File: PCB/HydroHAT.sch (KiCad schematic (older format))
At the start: 13 parts, among them IC1 ATMEGA1284P-P, P1 CONN_20X2, P2 CONN_4, P3 CONN_4, P4 CONN_10X2, P5 CONN_8, P6 CONN_4, SW1 SW_PUSH

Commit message: Changed Things
Stuff
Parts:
- removed P2, P3: CONN_4, symbol CONN_4
- added P2, P3: CONN_3, symbol CONN_3
- RES?: value RESONATOR_C -> 20MHz; Distrib Link (none) -> 490-1215-ND; Distrib PN (none) -> 490-1215-ND; MFG Name (none) -> Murata Electronics North America; MFG Part Num (none) -> CSTLS20M0X53-B0
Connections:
- net GND: now also P2.2 (PM), P3.2 (PM)
- net at IC1.22 ((PCINT16/SCL)PC0): now also P2.1 (P1)
- net at IC1.23 ((PCINT17/SDA)PC1): now also P2.3 (P3)
- net Vdd: now reaches P1.17 (P17)
- net at P1.3 (P3): now also P3.3 (P3)
- net at P1.5 (P5): now also P3.1 (P1)
- net MISO renamed MISO33
- net MISO33: no longer IC1.7 ((PCINT14/MISO)PB6)
- net MOSI renamed MOSI33
- net MOSI33: no longer IC1.6 ((PCINT13/MOSI)PB5)
- net SCK renamed SCK33
- net SCK33: no longer IC1.8 ((PCINT15/SCK)PB7)
- new net MISO50: IC1.7 ((PCINT14/MISO)PB6)
- new net MOSI50: IC1.6 ((PCINT13/MOSI)PB5)
- new net SCK50: IC1.8 ((PCINT15/SCK)PB7)
- no-connect marks 28 -> 27
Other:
- note added: "5V\nGPIO Port"
- note added: "To RPi\n 3.3V\n\n"
- note removed: "GPIO Port"
- note removed: "To RPi\n"
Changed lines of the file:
@@
 $EndComp
 Text Notes 9200 6200 0    60   ~ 12
-To RPi\n
+To RPi\n 3.3V\n\n
 Text GLabel 6350 4750 2    60   Input ~ 0
 RXD
@@
 P 4000 2650
 F 0 "RES?" H 4000 3000 60  0000 C CNN
-F 1 "RESONATOR_C" H 4000 2300 60  0000 C CNN
+F 1 "20MHz" H 4000 2300 60  0000 C CNN
 F 2 "" H 4000 3050 60  0000 C CNN
-F 3 "" H 4000 3050 60  0000 C CNN
+F 3 "http://www.murata.com/~/media/webrenewal/support/library/catalog/products/timingdevice/ceralock/p16e.ashx" H 4000 3050 60  0001 C CNN
+F 4 "Murata Electronics North America" H 4000 2650 60  0001 C CNN "MFG Name"
+F 5 "CSTLS20M0X53-B0" H 4000 2650 60  0001 C CNN "MFG Part Num"
+F 6 "490-1215-ND" H 4000 2650 60  0001 C CNN "Distrib PN"
+F 7 "490-1215-ND" H 4000 2650 60  0001 C CNN "Distrib Link"
 	1    4000 2650
 	1    0    0    -1
@@
 Text Notes 6900 5300 0    60   ~ 0
 Aux Serial Port
-Text Notes 6750 1750 0    60   ~ 0
-GPIO Port
-$Comp
-L CONN_4 P2
-U 1 1 5420C6D0
-P 7250 3900
-F 0 "P2" V 7200 3900 50  0000 C CNN
-F 1 "CONN_4" V 7300 3900 50  0000 C CNN
-F 2 "" H 7250 3900 60  0000 C CNN
-F 3 "" H 7250 3900 60  0000 C CNN
-	1    7250 3900
-	1    0    0    -1
-$EndComp
+Text Notes 6650 1750 0    60   ~ 0
+   5V\nGPIO Port
 Text Notes 6950 3650 0    60   ~ 0
 I2C Port
 Text GLabel 6350 3450 2    60   Input ~ 0
-MOSI
+MOSI50
 Text GLabel 6350 3550 2    60   Input ~ 0
-MISO
+MISO50
 Text GLabel 6350 3650 2    60   Input ~ 0
-SCK
+SCK50
 $Comp
 L C C3
@@
 Text GLabel 8950 4400 0    60   Input ~ 0
 GPIO4
-$Comp
-L CONN_4 P3
-U 1 1 5420C88A
-P 7950 4250
-F 0 "P3" V 7900 4250 50  0000 C CNN
-F 1 "CONN_4" V 8000 4250 50  0000 C CNN
-F 2 "" H 7950 4250 60  0000 C CNN
-F 3 "" H 7950 4250 60  0000 C CNN
-	1    7950 4250
-	-1   0    0    1
-$EndComp
 Text Notes 7850 4000 0    60   ~ 0
 RPi I2C Port\n
 Text GLabel 8950 5000 0    60   Input ~ 0
-MOSI
+MOSI33
 Text GLabel 8950 5100 0    60   Input ~ 0
-MISO
+MISO33
 Text GLabel 8950 5200 0    60   Input ~ 0
-SCK
+SCK33
 Text GLabel 9750 4400 2    60   Input ~ 0
 STX
@@
 	6900 5050 6350 5050
 Wire Wire Line
-	6900 3850 6350 3850
-Wire Wire Line
 	6350 3950 6900 3950
 Wire Wire Line
@@
 NoConn ~ 8950 4800
 NoConn ~ 8950 4100
-NoConn ~ 8950 4900
 NoConn ~ 8950 5300
 NoConn ~ 8950 5500
@@
 NoConn ~ 9750 5000
 Wire Wire Line
-	8950 4200 8300 4200
-Wire Wire Line
 	8300 4300 8950 4300
 Wire Wire Line
@@
 Text GLabel 7250 2850 2    60   Input ~ 0
 GND
+Wire Notes Line
+	9200 6200 9500 6200
+Wire Notes Line
+	9500 6200 9500 6300
+Wire Notes Line
+	9500 6300 9200 6300
+Wire Notes Line
+	9200 6300 9200 6200
+Wire Notes Line
+	6750 1650 6750 1750
+Wire Notes Line
+	6750 1750 6950 1750
+Wire Notes Line
+	6950 1750 6950 1650
+Wire Notes Line
+	6950 1650 6750 1650
+$Comp
+L CONN_3 P2
+U 1 1 5420F12C
+P 7250 3850
+F 0 "P2" V 7200 3850 50  0000 C CNN
+F 1 "CONN_3" V 7300 3850 40  0000 C CNN
+F 2 "" H 7250 3850 60  0000 C CNN
+F 3 "" H 7250 3850 60  0000 C CNN
+	1    7250 3850
+	1    0    0    -1
+$EndComp
+$Comp
+L CONN_3 P3
+U 1 1 5420F13B
+P 7950 4200
+F 0 "P3" V 7900 4200 50  0000 C CNN
+F 1 "CONN_3" V 8000 4200 40  0000 C CNN
+F 2 "" H 7950 4200 60  0000 C CNN
+F 3 "" H 7950 4200 60  0000 C CNN
+	1    7950 4200
+	-1   0    0    1
+$EndComp
+Wire Wire Line
+	8950 4200 8600 4200
+Wire Wire Line
+	8600 4200 8600 4100
+Wire Wire Line
+	8600 4100 8300 4100
+Text GLabel 8300 4200 2    60   Input ~ 0
+GND
+Text GLabel 6900 3850 0    60   Input ~ 0
+GND
+Wire Wire Line
+	6350 3850 6600 3850
+Wire Wire Line
+	6600 3850 6600 3750
+Wire Wire Line
+	6600 3750 6900 3750
+Text GLabel 8950 4900 0    60   Input ~ 0
+Vdd
 $EndSCHEMATC

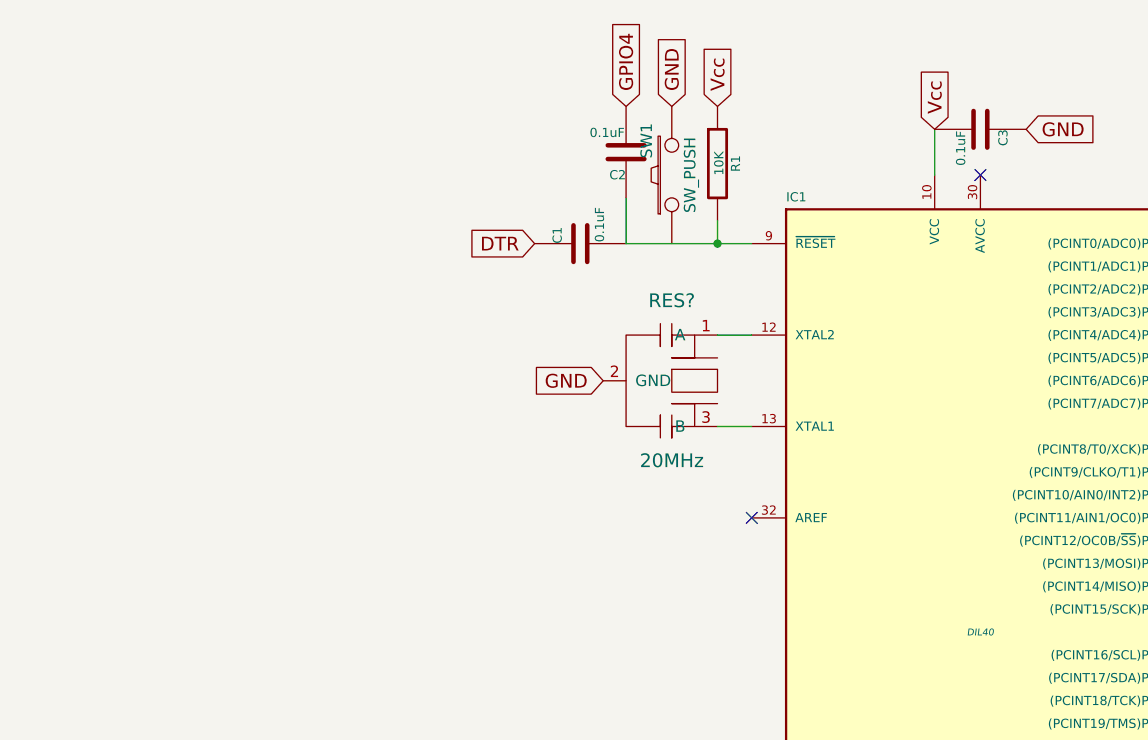
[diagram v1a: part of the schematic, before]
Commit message: Added level shifting to schematic
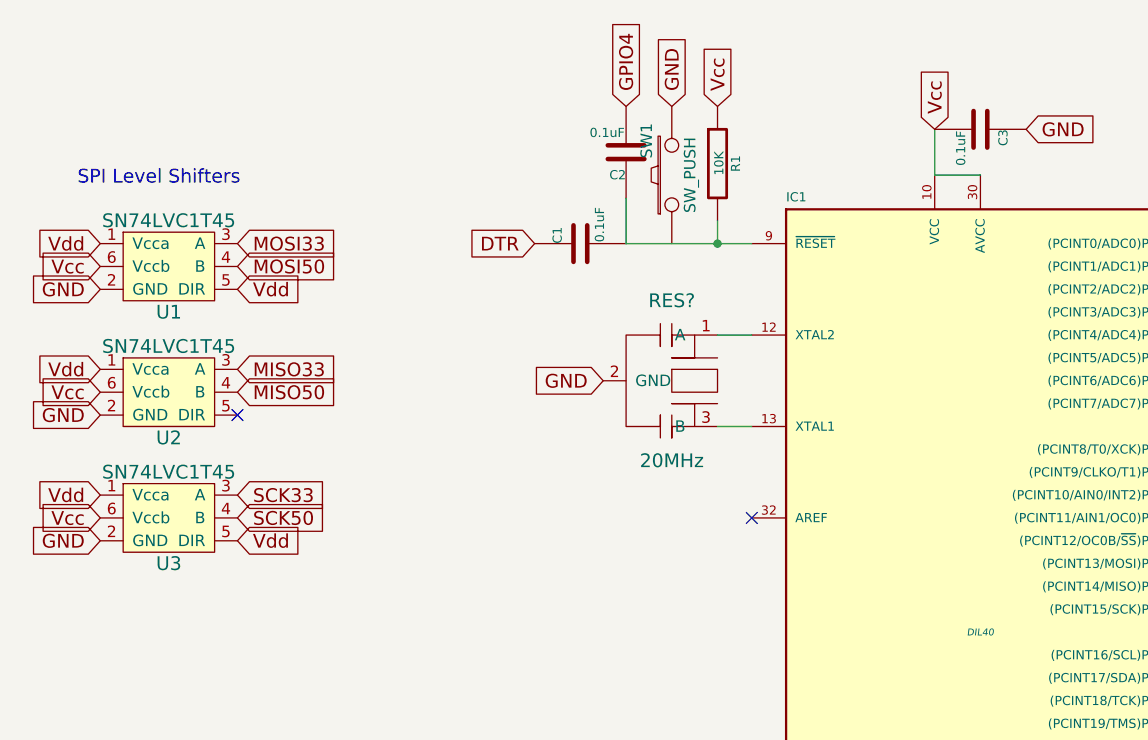
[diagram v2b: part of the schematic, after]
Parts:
- added U1, U2, U3: SN74LVC1T45, symbol SN74LVC1T45
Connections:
- net GND: now also U1.2 (GND), U2.2 (GND), U3.2 (GND)
- net MISO33: now also U2.3 (A)
- net MISO50: now also U2.4 (B)
- net MOSI33: now also U1.3 (A)
- net MOSI50: now also U1.4 (B)
- net SCK33: now also U3.3 (A)
- net SCK50: now also U3.4 (B)
- net Vcc: now also IC1.30 (AVCC), U1.6 (Vccb), U2.6 (Vccb), U3.6 (Vccb)
- net Vdd: now also U1.1 (Vcca), U1.5 (DIR), U2.1 (Vcca), U3.1 (Vcca), U3.5 (DIR)
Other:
- note added: "SPI Level Shifters"
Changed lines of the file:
@@
 Text GLabel 5350 5750 3    60   Input ~ 0
 GND
-NoConn ~ 5350 1750
-NoConn ~ 4350 3250
 NoConn ~ 6350 4150
 NoConn ~ 6350 4050
@@
 Text GLabel 8950 4900 0    60   Input ~ 0
 Vdd
+Wire Wire Line
+	5150 1750 5350 1750
+NoConn ~ 4350 3250
+$Comp
+L SN74LVC1T45 U1
+U 1 1 54219896
+P 1800 2150
+F 0 "U1" H 1800 1950 60  0000 C CNN
+F 1 "SN74LVC1T45" H 1800 2350 60  0000 C CNN
+F 2 "" H 1800 2150 60  0000 C CNN
+F 3 "" H 1800 2150 60  0000 C CNN
+	1    1800 2150
+	1    0    0    -1
+$EndComp
+$Comp
+L SN74LVC1T45 U2
+U 1 1 542198A3
+P 1800 2700
+F 0 "U2" H 1800 2500 60  0000 C CNN
+F 1 "SN74LVC1T45" H 1800 2900 60  0000 C CNN
+F 2 "" H 1800 2700 60  0000 C CNN
+F 3 "" H 1800 2700 60  0000 C CNN
+	1    1800 2700
+	1    0    0    -1
+$EndComp
+$Comp
+L SN74LVC1T45 U3
+U 1 1 542198A9
+P 1800 3250
+F 0 "U3" H 1800 3050 60  0000 C CNN
+F 1 "SN74LVC1T45" H 1800 3450 60  0000 C CNN
+F 2 "" H 1800 3250 60  0000 C CNN
+F 3 "" H 1800 3250 60  0000 C CNN
+	1    1800 3250
+	1    0    0    -1
+$EndComp
+Text Notes 1400 1800 0    60   ~ 0
+SPI Level Shifters
+Text GLabel 2100 2050 2    60   Input ~ 0
+MOSI33
+Text GLabel 2100 2150 2    60   Input ~ 0
+MOSI50
+Text GLabel 2100 2600 2    60   Input ~ 0
+MISO33
+Text GLabel 2100 2700 2    60   Input ~ 0
+MISO50
+Text GLabel 2100 3150 2    60   Input ~ 0
+SCK33
+Text GLabel 2100 3250 2    60   Input ~ 0
+SCK50
+Text GLabel 2100 2250 2    60   Input ~ 0
+Vdd
+NoConn ~ 2100 2800
+Text GLabel 1500 2050 0    60   Input ~ 0
+Vdd
+Text GLabel 1500 2600 0    60   Input ~ 0
+Vdd
+Text GLabel 1500 3150 0    60   Input ~ 0
+Vdd
+Text GLabel 1500 2150 0    60   Input ~ 0
+Vcc
+Text GLabel 1500 2700 0    60   Input ~ 0
+Vcc
+Text GLabel 1500 3250 0    60   Input ~ 0
+Vcc
+Text GLabel 1500 2250 0    60   Input ~ 0
+GND
+Text GLabel 1500 2800 0    60   Input ~ 0
+GND
+Text GLabel 1500 3350 0    60   Input ~ 0
+GND
+Text GLabel 2100 3350 2    60   Input ~ 0
+Vdd
 $EndSCHEMATC
